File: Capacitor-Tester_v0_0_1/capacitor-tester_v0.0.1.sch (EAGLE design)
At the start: 19 parts, among them IC1 AD8531ARZ, J1 USB4125-GF-A-0190_REVA2, J2 DS1044-140G, U1 AD5933, U2 LM6171AIMX/NOPB, Y1 LFSPXO018034

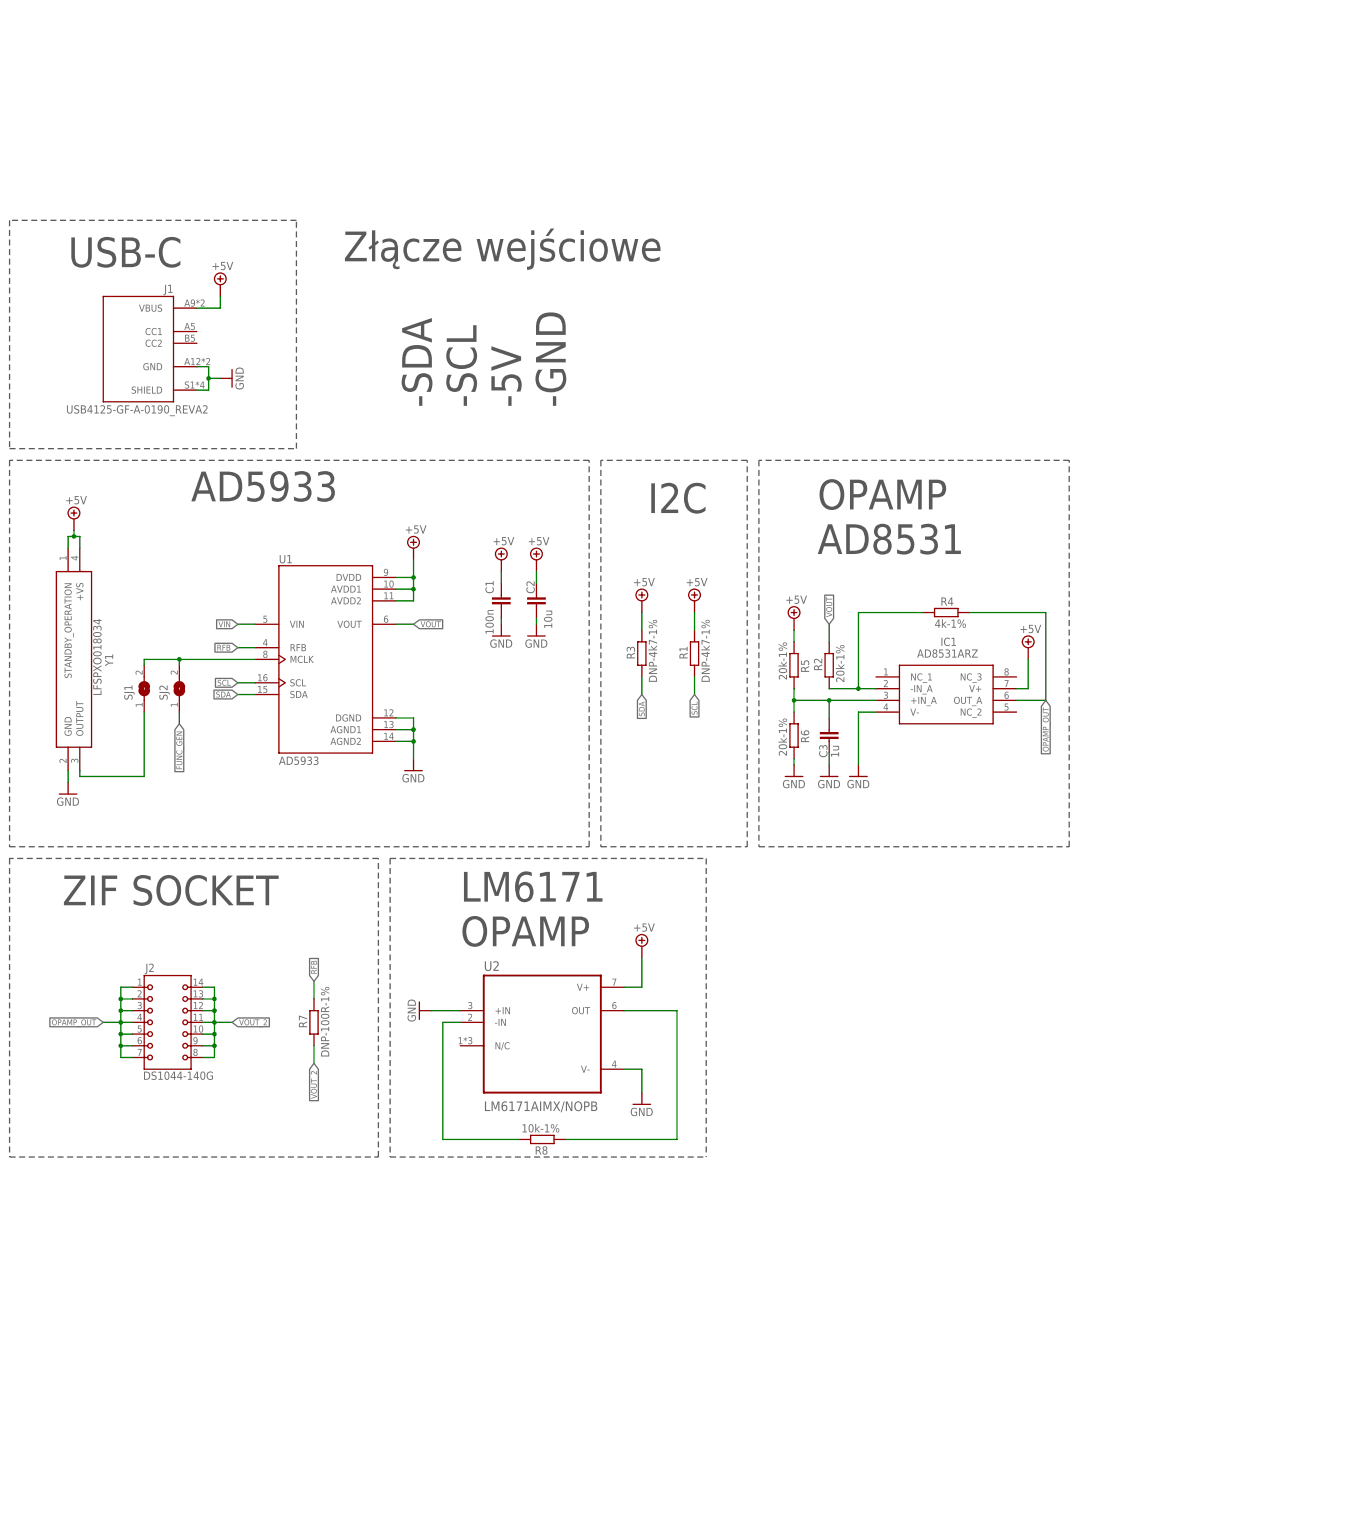
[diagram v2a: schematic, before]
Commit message: v0.0.1 - Added 5V -> 15V boost converter for the second stage opamp.
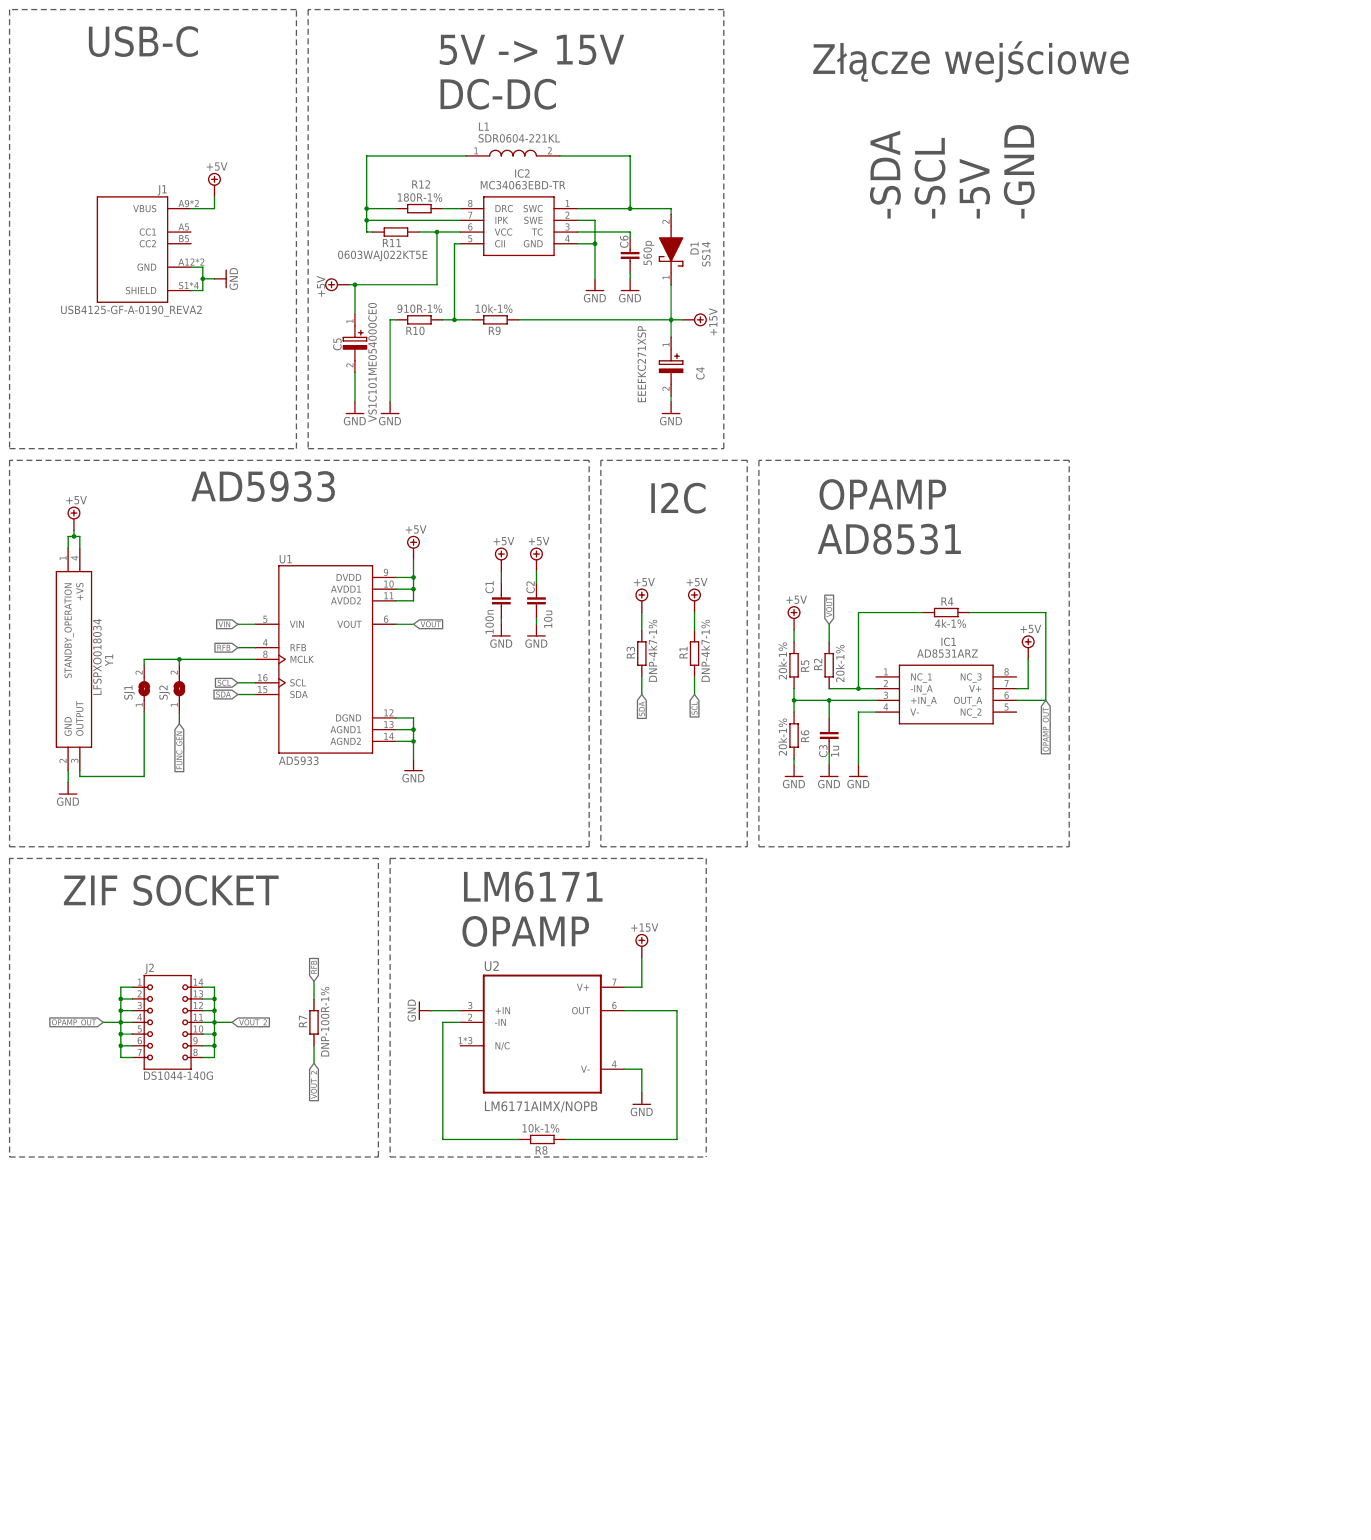
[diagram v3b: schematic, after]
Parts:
- added C4: EEEFKC271XSP, EEEFKC271XSP:EEEFKC271XSP
- added C5: VS1C101ME054000CE0, EEEFKC271XSP:EEEFKC271XSP
- added C6: 560p, custom_library:CAPACITOR_SMD_CERAMIC0603
- added D1: SS14, SS14:SS14
- added IC2: MC34063EBD-TR, MC34063EBD-TR:MC34063EBD-TR
- added L1: SDR0604-221KL, SDR0604-221KL:SDR0604-221KL
- added R10: 910R-1%, custom_library:RESISTOR_SMD0603
- added R11: 0603WAJ022KT5E, custom_library:RESISTOR_SMD0603
- added R12: 180R-1%, custom_library:RESISTOR_SMD0603
- added R9: 10k-1%, custom_library:RESISTOR_SMD0603
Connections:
- new net +15V: C4.+, D1.K, R9.1, U2.V+
- new net N$10: C6.1, IC2.TC
- new net N$11: IC2.IPK, L1.1, R11.2, R12.2
- new net N$5: D1.A, IC2.SWC, L1.2
- new net N$7: IC2.CII, R10.1, R9.2
- new net N$8: IC2.DRC, R12.1
- net +5V: now also C5.+, IC2.VCC, R11.1; no longer U2.V+
- net GND: now also C4.-, C5.-, C6.2, IC2.GND, IC2.SWE, R10.2
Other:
- note added: "5V -> 15V DC-DC"
- moved on the sheet: J1

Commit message: v0.0.1 - Added input connector
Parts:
- added J3: 250-102, custom_library:250-102
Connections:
- net SCL: now also J3.2
- net SDA: now also J3.1
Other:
- note added: "Input Connector"
- note removed: "-SDA -SCL -5V -GND"
- note removed: "Złącze wejściowe"
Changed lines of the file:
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@@
 <part name="SUPPLY12" library="supply2" library_urn="urn:adsk.eagle:library:372" deviceset="+5V" device=""/>
 <part name="SUPPLY10" library="supply2" library_urn="urn:adsk.eagle:library:372" deviceset="+15V" device=""/>
+<part name="J3" library="custom_library" deviceset="250-102" device=""/>
 </parts>
 <sheets>
@@
 <wire x1="-30.48" y1="71.12" x2="-30.48" y2="166.37" width="0.1524" layer="97" style="longdash"/>
 <wire x1="-30.48" y1="166.37" x2="-92.71" y2="166.37" width="0.1524" layer="97" style="longdash"/>
-<text x="81.28" y="152.4" size="6.4516" layer="97" ratio="16">Złącze wejściowe</text>
+<text x="67.31" y="146.05" size="6.4516" layer="97" ratio="16">Input
+Connector</text>
 <text x="45.72" y="57.15" size="6.4516" layer="97" ratio="16">I2C</text>
 <wire x1="35.56" y1="68.58" x2="35.56" y2="-15.24" width="0.1524" layer="97" style="longdash"/>
@@
 <wire x1="67.31" y1="-15.24" x2="67.31" y2="68.58" width="0.1524" layer="97" style="longdash"/>
 <wire x1="67.31" y1="68.58" x2="35.56" y2="68.58" width="0.1524" layer="97" style="longdash"/>
-<text x="129.54" y="120.65" size="6.4516" layer="97" ratio="16" rot="R90">-SDA
--SCL
--5V
--GND</text>
 <text x="82.55" y="48.26" size="6.4516" layer="97" ratio="16">OPAMP
 AD8531</text>
@@
 <wire x1="62.23" y1="71.12" x2="62.23" y2="166.37" width="0.1524" layer="97" style="longdash"/>
 <wire x1="62.23" y1="166.37" x2="-27.94" y2="166.37" width="0.1524" layer="97" style="longdash"/>
+<wire x1="64.77" y1="166.37" x2="64.77" y2="71.12" width="0.1524" layer="97" style="longdash"/>
+<wire x1="64.77" y1="71.12" x2="110.49" y2="71.12" width="0.1524" layer="97" style="longdash"/>
+<wire x1="110.49" y1="71.12" x2="110.49" y2="166.37" width="0.1524" layer="97" style="longdash"/>
+<wire x1="110.49" y1="166.37" x2="64.77" y2="166.37" width="0.1524" layer="97" style="longdash"/>
 </plain>
 <instances>
@@
 <instance part="SUPPLY10" gate="+15V" x="44.45" y="-36.83" smashed="yes">
 <attribute name="VALUE" x="41.91" y="-33.655" size="1.778" layer="96"/>
+</instance>
+<instance part="J3" gate="A" x="87.63" y="119.38" smashed="yes" rot="MR0">
+<attribute name="NAME" x="83.4644" y="124.6886" size="2.0828" layer="95" ratio="6" rot="SMR0"/>
 </instance>
 </instances>
@@
 <label x="55.88" y="17.78" size="1.27" layer="95" rot="R270" xref="yes"/>
 </segment>
+<segment>
+<pinref part="J3" gate="A" pin="2"/>
+<wire x1="87.63" y1="116.84" x2="91.44" y2="116.84" width="0.1524" layer="91"/>
+<label x="91.44" y="116.84" size="1.27" layer="95" rot="MR180" xref="yes"/>
+</segment>
 </net>
 <net name="SDA" class="0">
@@
 <label x="44.45" y="17.78" size="1.27" layer="95" rot="R270" xref="yes"/>
 </segment>
+<segment>
+<pinref part="J3" gate="A" pin="1"/>
+<wire x1="87.63" y1="119.38" x2="91.44" y2="119.38" width="0.1524" layer="91"/>
+<label x="91.44" y="119.38" size="1.27" layer="95" rot="MR180" xref="yes"/>
+</segment>
 </net>

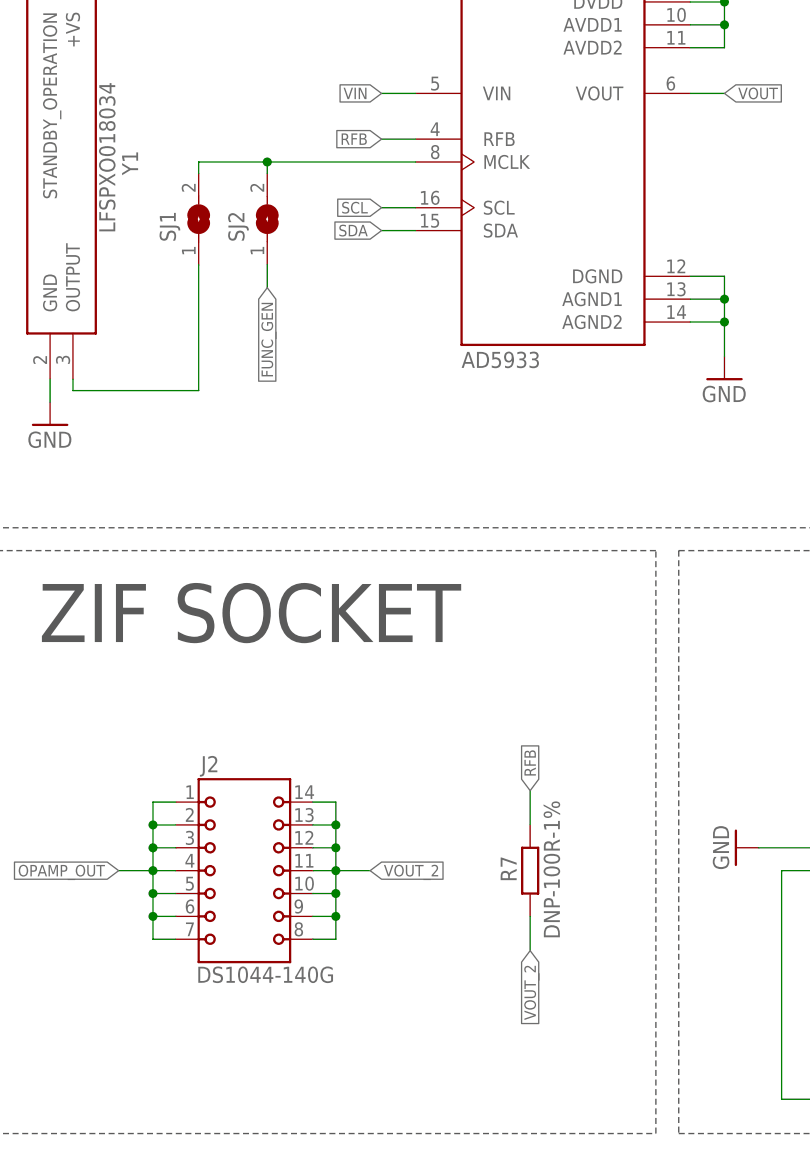
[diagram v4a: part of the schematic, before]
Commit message: v0.0.1 - Fix in the schematic. Bad label. Version before changing the input connector to Wago 250-103
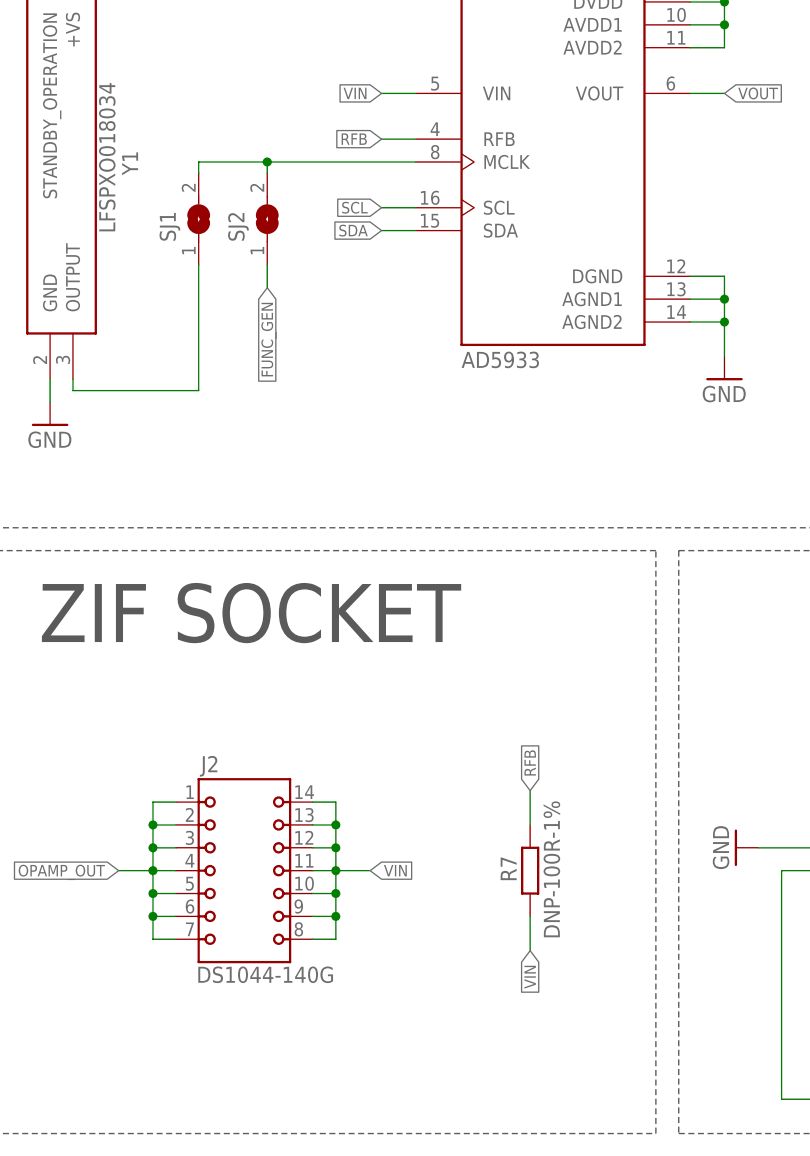
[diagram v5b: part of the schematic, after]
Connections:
- removed net VOUT_2: J2.10, J2.11, J2.12, J2.13, J2.14, J2.8, J2.9, R7.1
- new net N$6: SJ1.2, SJ2.2, U1.MCLK
- net MCLK: no longer SJ1.2, SJ2.2, U1.MCLK
- net VIN: now also J2.10, J2.11, J2.12, J2.13, J2.14, J2.8, J2.9, R7.1
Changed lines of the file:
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@@
 <wire x1="-63.5" y1="0" x2="-63.5" y2="13.97" width="0.1524" layer="91"/>
-</segment>
-<segment>
-<pinref part="U1" gate="G$1" pin="MCLK"/>
-<pinref part="SJ1" gate="1" pin="2"/>
-<wire x1="-63.5" y1="24.13" x2="-63.5" y2="25.4" width="0.1524" layer="91"/>
-<wire x1="-63.5" y1="25.4" x2="-55.88" y2="25.4" width="0.1524" layer="91"/>
-<pinref part="SJ2" gate="1" pin="2"/>
-<wire x1="-55.88" y1="25.4" x2="-39.37" y2="25.4" width="0.1524" layer="91"/>
-<wire x1="-55.88" y1="24.13" x2="-55.88" y2="25.4" width="0.1524" layer="91"/>
-<junction x="-55.88" y="25.4"/>
 </segment>
 </net>
@@
 <wire x1="-39.37" y1="33.02" x2="-43.18" y2="33.02" width="0.1524" layer="91"/>
 <label x="-43.18" y="33.02" size="1.27" layer="95" rot="R180" xref="yes"/>
+</segment>
+<segment>
+<pinref part="J2" gate="G$1" pin="14"/>
+<wire x1="-50.8" y1="-45.72" x2="-48.26" y2="-45.72" width="0.1524" layer="91"/>
+<wire x1="-48.26" y1="-45.72" x2="-48.26" y2="-48.26" width="0.1524" layer="91"/>
+<pinref part="J2" gate="G$1" pin="13"/>
+<wire x1="-48.26" y1="-48.26" x2="-50.8" y2="-48.26" width="0.1524" layer="91"/>
+<wire x1="-48.26" y1="-48.26" x2="-48.26" y2="-50.8" width="0.1524" layer="91"/>
+<junction x="-48.26" y="-48.26"/>
+<pinref part="J2" gate="G$1" pin="12"/>
+<wire x1="-48.26" y1="-50.8" x2="-50.8" y2="-50.8" width="0.1524" layer="91"/>
+<pinref part="J2" gate="G$1" pin="8"/>
+<wire x1="-48.26" y1="-50.8" x2="-48.26" y2="-53.34" width="0.1524" layer="91"/>
+<wire x1="-48.26" y1="-53.34" x2="-48.26" y2="-55.88" width="0.1524" layer="91"/>
+<wire x1="-48.26" y1="-55.88" x2="-48.26" y2="-58.42" width="0.1524" layer="91"/>
+<wire x1="-48.26" y1="-58.42" x2="-48.26" y2="-60.96" width="0.1524" layer="91"/>
+<wire x1="-48.26" y1="-60.96" x2="-50.8" y2="-60.96" width="0.1524" layer="91"/>
+<junction x="-48.26" y="-50.8"/>
+<pinref part="J2" gate="G$1" pin="11"/>
+<wire x1="-50.8" y1="-53.34" x2="-48.26" y2="-53.34" width="0.1524" layer="91"/>
+<junction x="-48.26" y="-53.34"/>
+<pinref part="J2" gate="G$1" pin="10"/>
+<wire x1="-50.8" y1="-55.88" x2="-48.26" y2="-55.88" width="0.1524" layer="91"/>
+<junction x="-48.26" y="-55.88"/>
+<pinref part="J2" gate="G$1" pin="9"/>
+<wire x1="-50.8" y1="-58.42" x2="-48.26" y2="-58.42" width="0.1524" layer="91"/>
+<junction x="-48.26" y="-58.42"/>
+<wire x1="-48.26" y1="-53.34" x2="-44.45" y2="-53.34" width="0.1524" layer="91"/>
+<label x="-44.45" y="-53.34" size="1.27" layer="95" xref="yes"/>
+</segment>
+<segment>
+<pinref part="R7" gate="G$1" pin="1"/>
+<wire x1="-26.67" y1="-58.42" x2="-26.67" y2="-62.23" width="0.1524" layer="91"/>
+<label x="-26.67" y="-62.23" size="1.27" layer="95" rot="R270" xref="yes"/>
 </segment>
 </net>
@@
 </segment>
 </net>
-<net name="VOUT_2" class="0">
-<segment>
-<pinref part="J2" gate="G$1" pin="14"/>
-<wire x1="-50.8" y1="-45.72" x2="-48.26" y2="-45.72" width="0.1524" layer="91"/>
-<wire x1="-48.26" y1="-45.72" x2="-48.26" y2="-48.26" width="0.1524" layer="91"/>
-<pinref part="J2" gate="G$1" pin="13"/>
-<wire x1="-48.26" y1="-48.26" x2="-50.8" y2="-48.26" width="0.1524" layer="91"/>
-<wire x1="-48.26" y1="-48.26" x2="-48.26" y2="-50.8" width="0.1524" layer="91"/>
-<junction x="-48.26" y="-48.26"/>
-<pinref part="J2" gate="G$1" pin="12"/>
-<wire x1="-48.26" y1="-50.8" x2="-50.8" y2="-50.8" width="0.1524" layer="91"/>
-<pinref part="J2" gate="G$1" pin="8"/>
-<wire x1="-48.26" y1="-50.8" x2="-48.26" y2="-53.34" width="0.1524" layer="91"/>
-<wire x1="-48.26" y1="-53.34" x2="-48.26" y2="-55.88" width="0.1524" layer="91"/>
-<wire x1="-48.26" y1="-55.88" x2="-48.26" y2="-58.42" width="0.1524" layer="91"/>
-<wire x1="-48.26" y1="-58.42" x2="-48.26" y2="-60.96" width="0.1524" layer="91"/>
-<wire x1="-48.26" y1="-60.96" x2="-50.8" y2="-60.96" width="0.1524" layer="91"/>
-<junction x="-48.26" y="-50.8"/>
-<pinref part="J2" gate="G$1" pin="11"/>
-<wire x1="-50.8" y1="-53.34" x2="-48.26" y2="-53.34" width="0.1524" layer="91"/>
-<junction x="-48.26" y="-53.34"/>
-<pinref part="J2" gate="G$1" pin="10"/>
-<wire x1="-50.8" y1="-55.88" x2="-48.26" y2="-55.88" width="0.1524" layer="91"/>
-<junction x="-48.26" y="-55.88"/>
-<pinref part="J2" gate="G$1" pin="9"/>
-<wire x1="-50.8" y1="-58.42" x2="-48.26" y2="-58.42" width="0.1524" layer="91"/>
-<junction x="-48.26" y="-58.42"/>
-<wire x1="-48.26" y1="-53.34" x2="-44.45" y2="-53.34" width="0.1524" layer="91"/>
-<label x="-44.45" y="-53.34" size="1.27" layer="95" xref="yes"/>
-</segment>
-<segment>
-<pinref part="R7" gate="G$1" pin="1"/>
-<wire x1="-26.67" y1="-58.42" x2="-26.67" y2="-62.23" width="0.1524" layer="91"/>
-<label x="-26.67" y="-62.23" size="1.27" layer="95" rot="R270" xref="yes"/>
-</segment>
-</net>
 <net name="N$2" class="0">
 <segment>
@@
 </segment>
 </net>
+<net name="N$6" class="0">
+<segment>
+<pinref part="SJ1" gate="1" pin="2"/>
+<wire x1="-63.5" y1="24.13" x2="-63.5" y2="25.4" width="0.1524" layer="91"/>
+<wire x1="-63.5" y1="25.4" x2="-55.88" y2="25.4" width="0.1524" layer="91"/>
+<pinref part="SJ2" gate="1" pin="2"/>
+<wire x1="-55.88" y1="25.4" x2="-55.88" y2="24.13" width="0.1524" layer="91"/>
+<pinref part="U1" gate="G$1" pin="MCLK"/>
+<wire x1="-55.88" y1="25.4" x2="-39.37" y2="25.4" width="0.1524" layer="91"/>
+<junction x="-55.88" y="25.4"/>
+</segment>
+</net>
